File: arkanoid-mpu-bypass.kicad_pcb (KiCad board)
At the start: 2 copper layers, 19.6 x 37.3 mm, 1 part, among them J1 DIP28

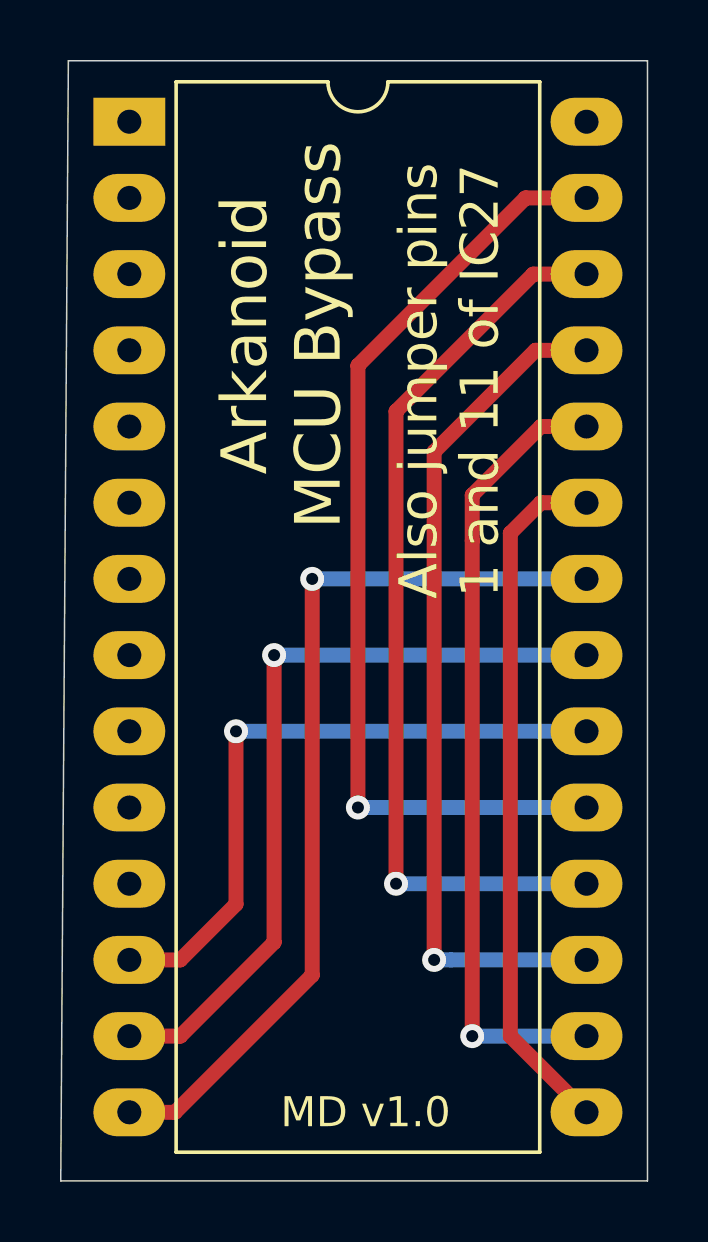
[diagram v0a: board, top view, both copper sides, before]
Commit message: Modified to use extra jumper.
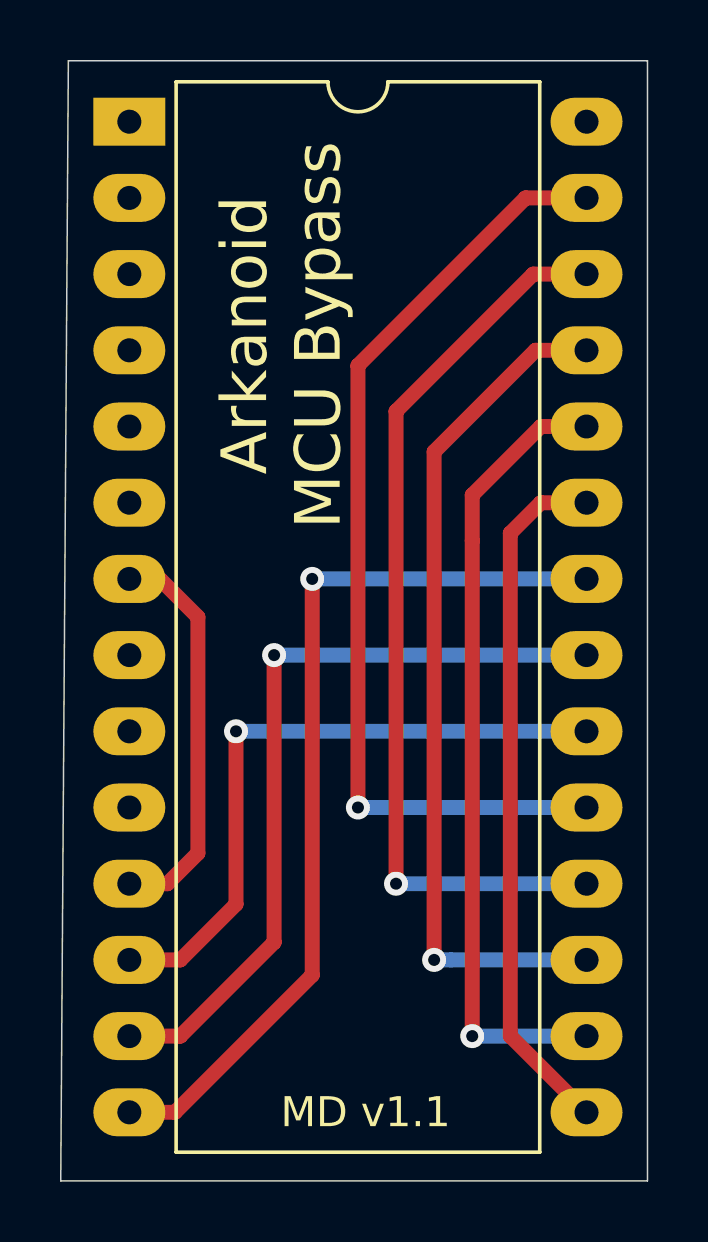
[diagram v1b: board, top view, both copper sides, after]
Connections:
- J1 pad 7: Net-(J1-Pad7) -> Net-(J1-Pad11)
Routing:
- net Net-(J1-Pad11): track 0.00 -> 13.4 mm
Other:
- board text added: "MD v1.1"
- board text removed: "Also jumper pins 1 and 11 of IC27"
- board text removed: "MD v1.0"
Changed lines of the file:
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@@
   (general
     (thickness 1.6)
-    (drawings 7)
-    (tracks 42)
+    (drawings 6)
+    (tracks 47)
     (zones 0)
     (modules 1)
-    (nets 21)
+    (nets 20)
   )
   (page USLetter)
   (title_block
     (title "Arkanoid MCU Bypass")
-    (date 2022-07-09)
-    (rev 1.0)
+    (date 2022-07-13)
+    (rev 1.1)
     (company "Marc Deslauriers")
   )
@@
   (net 12 "Net-(J1-Pad9)")
   (net 13 "Net-(J1-Pad8)")
-  (net 14 "Net-(J1-Pad7)")
-  (net 15 "Net-(J1-Pad6)")
-  (net 16 "Net-(J1-Pad5)")
-  (net 17 "Net-(J1-Pad4)")
-  (net 18 "Net-(J1-Pad3)")
-  (net 19 "Net-(J1-Pad2)")
-  (net 20 "Net-(J1-Pad1)")
+  (net 14 "Net-(J1-Pad6)")
+  (net 15 "Net-(J1-Pad5)")
+  (net 16 "Net-(J1-Pad4)")
+  (net 17 "Net-(J1-Pad3)")
+  (net 18 "Net-(J1-Pad2)")
+  (net 19 "Net-(J1-Pad1)")
   (net_class Default "This is the default net class."
     (clearance 0.2)
@@
     (add_net "Net-(J1-Pad5)")
     (add_net "Net-(J1-Pad6)")
-    (add_net "Net-(J1-Pad7)")
     (add_net "Net-(J1-Pad8)")
     (add_net "Net-(J1-Pad9)")
@@
       (effects (font (size 1 1) (thickness 0.15)))
     )
+    (fp_line (start 16.7 -1.55) (end -1.5 -1.55) (layer F.CrtYd) (width 0.05))
+    (fp_line (start 16.7 34.55) (end 16.7 -1.55) (layer F.CrtYd) (width 0.05))
+    (fp_line (start -1.5 34.55) (end 16.7 34.55) (layer F.CrtYd) (width 0.05))
+    (fp_line (start -1.5 -1.55) (end -1.5 34.55) (layer F.CrtYd) (width 0.05))
+    (fp_line (start 13.68 -1.33) (end 8.62 -1.33) (layer F.SilkS) (width 0.12))
+    (fp_line (start 13.68 34.35) (end 13.68 -1.33) (layer F.SilkS) (width 0.12))
+    (fp_line (start 1.56 34.35) (end 13.68 34.35) (layer F.SilkS) (width 0.12))
+    (fp_line (start 1.56 -1.33) (end 1.56 34.35) (layer F.SilkS) (width 0.12))
+    (fp_line (start 6.62 -1.33) (end 1.56 -1.33) (layer F.SilkS) (width 0.12))
+    (fp_line (start 0.255 -0.27) (end 1.255 -1.27) (layer F.Fab) (width 0.1))
+    (fp_line (start 0.255 34.29) (end 0.255 -0.27) (layer F.Fab) (width 0.1))
+    (fp_line (start 14.985 34.29) (end 0.255 34.29) (layer F.Fab) (width 0.1))
+    (fp_line (start 14.985 -1.27) (end 14.985 34.29) (layer F.Fab) (width 0.1))
+    (fp_line (start 1.255 -1.27) (end 14.985 -1.27) (layer F.Fab) (width 0.1))
     (fp_text user %R (at 7.62 16.51) (layer F.Fab) hide
       (effects (font (size 1 1) (thickness 0.15)))
     )
     (fp_arc (start 7.62 -1.33) (end 6.62 -1.33) (angle -180) (layer F.SilkS) (width 0.12))
-    (fp_line (start 1.255 -1.27) (end 14.985 -1.27) (layer F.Fab) (width 0.1))
-    (fp_line (start 14.985 -1.27) (end 14.985 34.29) (layer F.Fab) (width 0.1))
-    (fp_line (start 14.985 34.29) (end 0.255 34.29) (layer F.Fab) (width 0.1))
-    (fp_line (start 0.255 34.29) (end 0.255 -0.27) (layer F.Fab) (width 0.1))
-    (fp_line (start 0.255 -0.27) (end 1.255 -1.27) (layer F.Fab) (width 0.1))
-    (fp_line (start 6.62 -1.33) (end 1.56 -1.33) (layer F.SilkS) (width 0.12))
-    (fp_line (start 1.56 -1.33) (end 1.56 34.35) (layer F.SilkS) (width 0.12))
-    (fp_line (start 1.56 34.35) (end 13.68 34.35) (layer F.SilkS) (width 0.12))
-    (fp_line (start 13.68 34.35) (end 13.68 -1.33) (layer F.SilkS) (width 0.12))
-    (fp_line (start 13.68 -1.33) (end 8.62 -1.33) (layer F.SilkS) (width 0.12))
-    (fp_line (start -1.5 -1.55) (end -1.5 34.55) (layer F.CrtYd) (width 0.05))
-    (fp_line (start -1.5 34.55) (end 16.7 34.55) (layer F.CrtYd) (width 0.05))
-    (fp_line (start 16.7 34.55) (end 16.7 -1.55) (layer F.CrtYd) (width 0.05))
-    (fp_line (start 16.7 -1.55) (end -1.5 -1.55) (layer F.CrtYd) (width 0.05))
     (pad 28 thru_hole oval (at 15.24 0) (size 2.4 1.6) (drill 0.8) (layers *.Cu *.Mask)
       (net 1 "Net-(J1-Pad28)"))
@@
       (net 4 "Net-(J1-Pad13)"))
     (pad 7 thru_hole oval (at 0 15.24) (size 2.4 1.6) (drill 0.8) (layers *.Cu *.Mask)
-      (net 14 "Net-(J1-Pad7)"))
+      (net 8 "Net-(J1-Pad11)"))
     (pad 20 thru_hole oval (at 15.24 20.32) (size 2.4 1.6) (drill 0.8) (layers *.Cu *.Mask)
       (net 6 "Net-(J1-Pad12)"))
     (pad 6 thru_hole oval (at 0 12.7) (size 2.4 1.6) (drill 0.8) (layers *.Cu *.Mask)
-      (net 15 "Net-(J1-Pad6)"))
+      (net 14 "Net-(J1-Pad6)"))
     (pad 19 thru_hole oval (at 15.24 22.86) (size 2.4 1.6) (drill 0.8) (layers *.Cu *.Mask)
       (net 3 "Net-(J1-Pad19)"))
     (pad 5 thru_hole oval (at 0 10.16) (size 2.4 1.6) (drill 0.8) (layers *.Cu *.Mask)
-      (net 16 "Net-(J1-Pad5)"))
+      (net 15 "Net-(J1-Pad5)"))
     (pad 18 thru_hole oval (at 15.24 25.4) (size 2.4 1.6) (drill 0.8) (layers *.Cu *.Mask)
       (net 5 "Net-(J1-Pad18)"))
     (pad 4 thru_hole oval (at 0 7.62) (size 2.4 1.6) (drill 0.8) (layers *.Cu *.Mask)
-      (net 17 "Net-(J1-Pad4)"))
+      (net 16 "Net-(J1-Pad4)"))
     (pad 17 thru_hole oval (at 15.24 27.94) (size 2.4 1.6) (drill 0.8) (layers *.Cu *.Mask)
       (net 7 "Net-(J1-Pad17)"))
     (pad 3 thru_hole oval (at 0 5.08) (size 2.4 1.6) (drill 0.8) (layers *.Cu *.Mask)
-      (net 18 "Net-(J1-Pad3)"))
+      (net 17 "Net-(J1-Pad3)"))
     (pad 16 thru_hole oval (at 15.24 30.48) (size 2.4 1.6) (drill 0.8) (layers *.Cu *.Mask)
       (net 9 "Net-(J1-Pad16)"))
     (pad 2 thru_hole oval (at 0 2.54) (size 2.4 1.6) (drill 0.8) (layers *.Cu *.Mask)
-      (net 19 "Net-(J1-Pad2)"))
+      (net 18 "Net-(J1-Pad2)"))
     (pad 15 thru_hole oval (at 15.24 33.02) (size 2.4 1.6) (drill 0.8) (layers *.Cu *.Mask)
       (net 11 "Net-(J1-Pad15)"))
     (pad 1 thru_hole rect (at 0 0) (size 2.4 1.6) (drill 0.8) (layers *.Cu *.Mask)
-      (net 20 "Net-(J1-Pad1)"))
+      (net 19 "Net-(J1-Pad1)"))
   )
   (gr_line (start 142.748 89.916) (end 143.002 52.578) (layer Edge.Cuts) (width 0.05))
@@
   (gr_line (start 162.306 52.578) (end 162.306 89.916) (layer Edge.Cuts) (width 0.05))
   (gr_line (start 143.002 52.578) (end 162.306 52.578) (layer Edge.Cuts) (width 0.05))
-  (gr_text "MD v1.0" (at 152.908 87.63) (layer F.SilkS)
+  (gr_text "MD v1.1" (at 152.908 87.63) (layer F.SilkS)
     (effects (font (size 1 1) (thickness 0.15)))
-  )
-  (gr_text "Also jumper pins\n1 and 11 of IC27" (at 155.702 63.246 90) (layer F.SilkS)
-    (effects (font (size 1.27 1.27) (thickness 0.15)))
   )
   (gr_text "Arkanoid\nMCU Bypass" (at 150.114 61.722 90) (layer F.SilkS)
@@
   (segment (start 160.274 62.23) (end 158.574 62.23) (width 0.5) (layer F.Cu) (net 7))
   (segment (start 155.194001 65.609999) (end 155.194001 82.550001) (width 0.5) (layer F.Cu) (net 7))
+  (segment (start 146.304 80.01) (end 145.034 80.01) (width 0.5) (layer F.Cu) (net 8))
+  (segment (start 147.32 78.994) (end 146.304 80.01) (width 0.5) (layer F.Cu) (net 8))
+  (segment (start 147.32 71.12) (end 147.32 78.994) (width 0.5) (layer F.Cu) (net 8))
+  (segment (start 146.05 69.85) (end 147.32 71.12) (width 0.5) (layer F.Cu) (net 8))
+  (segment (start 145.034 69.85) (end 146.05 69.85) (width 0.5) (layer F.Cu) (net 8))
   (segment (start 156.464 68.58) (end 156.464 85.09) (width 0.5) (layer F.Cu) (net 9))
   (via (at 156.464 85.09) (size 0.8) (drill 0.4) (layers F.Cu B.Cu) (net 9))

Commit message: Rotated text the right way on the PCB
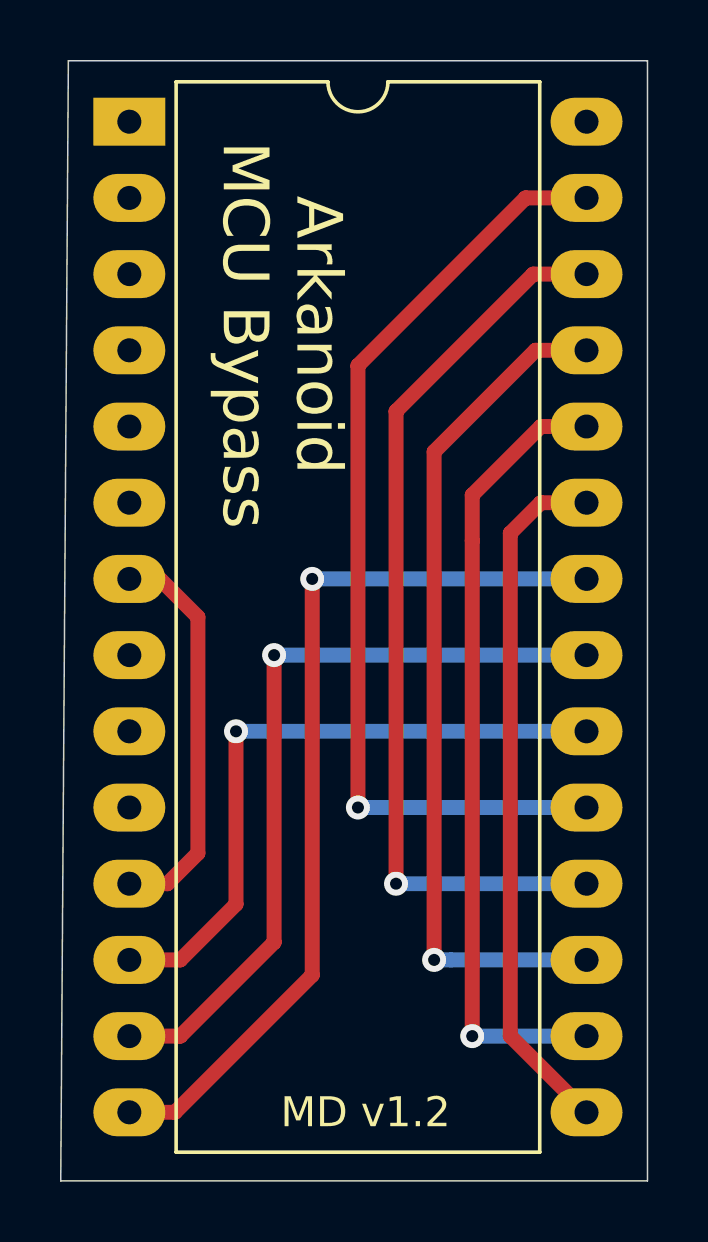
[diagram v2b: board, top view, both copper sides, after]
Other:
- board text added: "MD v1.2"
- board text removed: "MD v1.1"
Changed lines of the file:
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@@
   (title_block
     (title "Arkanoid MCU Bypass")
-    (date 2022-07-13)
-    (rev 1.1)
+    (date 2022-07-29)
+    (rev 1.2)
     (company "Marc Deslauriers")
   )
@@
   )
   (setup
-    (last_trace_width 0.5)
+    (last_trace_width 0.25)
     (user_trace_width 0.5)
     (trace_clearance 0.2)
@@
       (effects (font (size 1 1) (thickness 0.15)))
     )
+    (fp_line (start 1.255 -1.27) (end 14.985 -1.27) (layer F.Fab) (width 0.1))
+    (fp_line (start 14.985 -1.27) (end 14.985 34.29) (layer F.Fab) (width 0.1))
+    (fp_line (start 14.985 34.29) (end 0.255 34.29) (layer F.Fab) (width 0.1))
+    (fp_line (start 0.255 34.29) (end 0.255 -0.27) (layer F.Fab) (width 0.1))
+    (fp_line (start 0.255 -0.27) (end 1.255 -1.27) (layer F.Fab) (width 0.1))
+    (fp_line (start 6.62 -1.33) (end 1.56 -1.33) (layer F.SilkS) (width 0.12))
+    (fp_line (start 1.56 -1.33) (end 1.56 34.35) (layer F.SilkS) (width 0.12))
+    (fp_line (start 1.56 34.35) (end 13.68 34.35) (layer F.SilkS) (width 0.12))
+    (fp_line (start 13.68 34.35) (end 13.68 -1.33) (layer F.SilkS) (width 0.12))
+    (fp_line (start 13.68 -1.33) (end 8.62 -1.33) (layer F.SilkS) (width 0.12))
+    (fp_line (start -1.5 -1.55) (end -1.5 34.55) (layer F.CrtYd) (width 0.05))
+    (fp_line (start -1.5 34.55) (end 16.7 34.55) (layer F.CrtYd) (width 0.05))
+    (fp_line (start 16.7 34.55) (end 16.7 -1.55) (layer F.CrtYd) (width 0.05))
     (fp_line (start 16.7 -1.55) (end -1.5 -1.55) (layer F.CrtYd) (width 0.05))
-    (fp_line (start 16.7 34.55) (end 16.7 -1.55) (layer F.CrtYd) (width 0.05))
-    (fp_line (start -1.5 34.55) (end 16.7 34.55) (layer F.CrtYd) (width 0.05))
-    (fp_line (start -1.5 -1.55) (end -1.5 34.55) (layer F.CrtYd) (width 0.05))
-    (fp_line (start 13.68 -1.33) (end 8.62 -1.33) (layer F.SilkS) (width 0.12))
-    (fp_line (start 13.68 34.35) (end 13.68 -1.33) (layer F.SilkS) (width 0.12))
-    (fp_line (start 1.56 34.35) (end 13.68 34.35) (layer F.SilkS) (width 0.12))
-    (fp_line (start 1.56 -1.33) (end 1.56 34.35) (layer F.SilkS) (width 0.12))
-    (fp_line (start 6.62 -1.33) (end 1.56 -1.33) (layer F.SilkS) (width 0.12))
-    (fp_line (start 0.255 -0.27) (end 1.255 -1.27) (layer F.Fab) (width 0.1))
-    (fp_line (start 0.255 34.29) (end 0.255 -0.27) (layer F.Fab) (width 0.1))
-    (fp_line (start 14.985 34.29) (end 0.255 34.29) (layer F.Fab) (width 0.1))
-    (fp_line (start 14.985 -1.27) (end 14.985 34.29) (layer F.Fab) (width 0.1))
-    (fp_line (start 1.255 -1.27) (end 14.985 -1.27) (layer F.Fab) (width 0.1))
     (fp_text user %R (at 7.62 16.51) (layer F.Fab) hide
       (effects (font (size 1 1) (thickness 0.15)))
@@
   (gr_line (start 162.306 52.578) (end 162.306 89.916) (layer Edge.Cuts) (width 0.05))
   (gr_line (start 143.002 52.578) (end 162.306 52.578) (layer Edge.Cuts) (width 0.05))
-  (gr_text "MD v1.1" (at 152.908 87.63) (layer F.SilkS)
+  (gr_text "MD v1.2" (at 152.908 87.63) (layer F.SilkS)
     (effects (font (size 1 1) (thickness 0.15)))
   )
-  (gr_text "Arkanoid\nMCU Bypass" (at 150.114 61.722 90) (layer F.SilkS)
+  (gr_text "Arkanoid\nMCU Bypass" (at 150.114 61.722 270) (layer F.SilkS)
     (effects (font (size 1.524 1.524) (thickness 0.15)))
   )
